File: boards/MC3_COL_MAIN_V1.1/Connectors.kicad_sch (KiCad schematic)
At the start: 11 parts, among them J13 HARNESS_FFC_6P, J3 ENC_leaf1, J4 ENC_leaf2, J5 ENC_leaf3, J6 ENC_leaf4

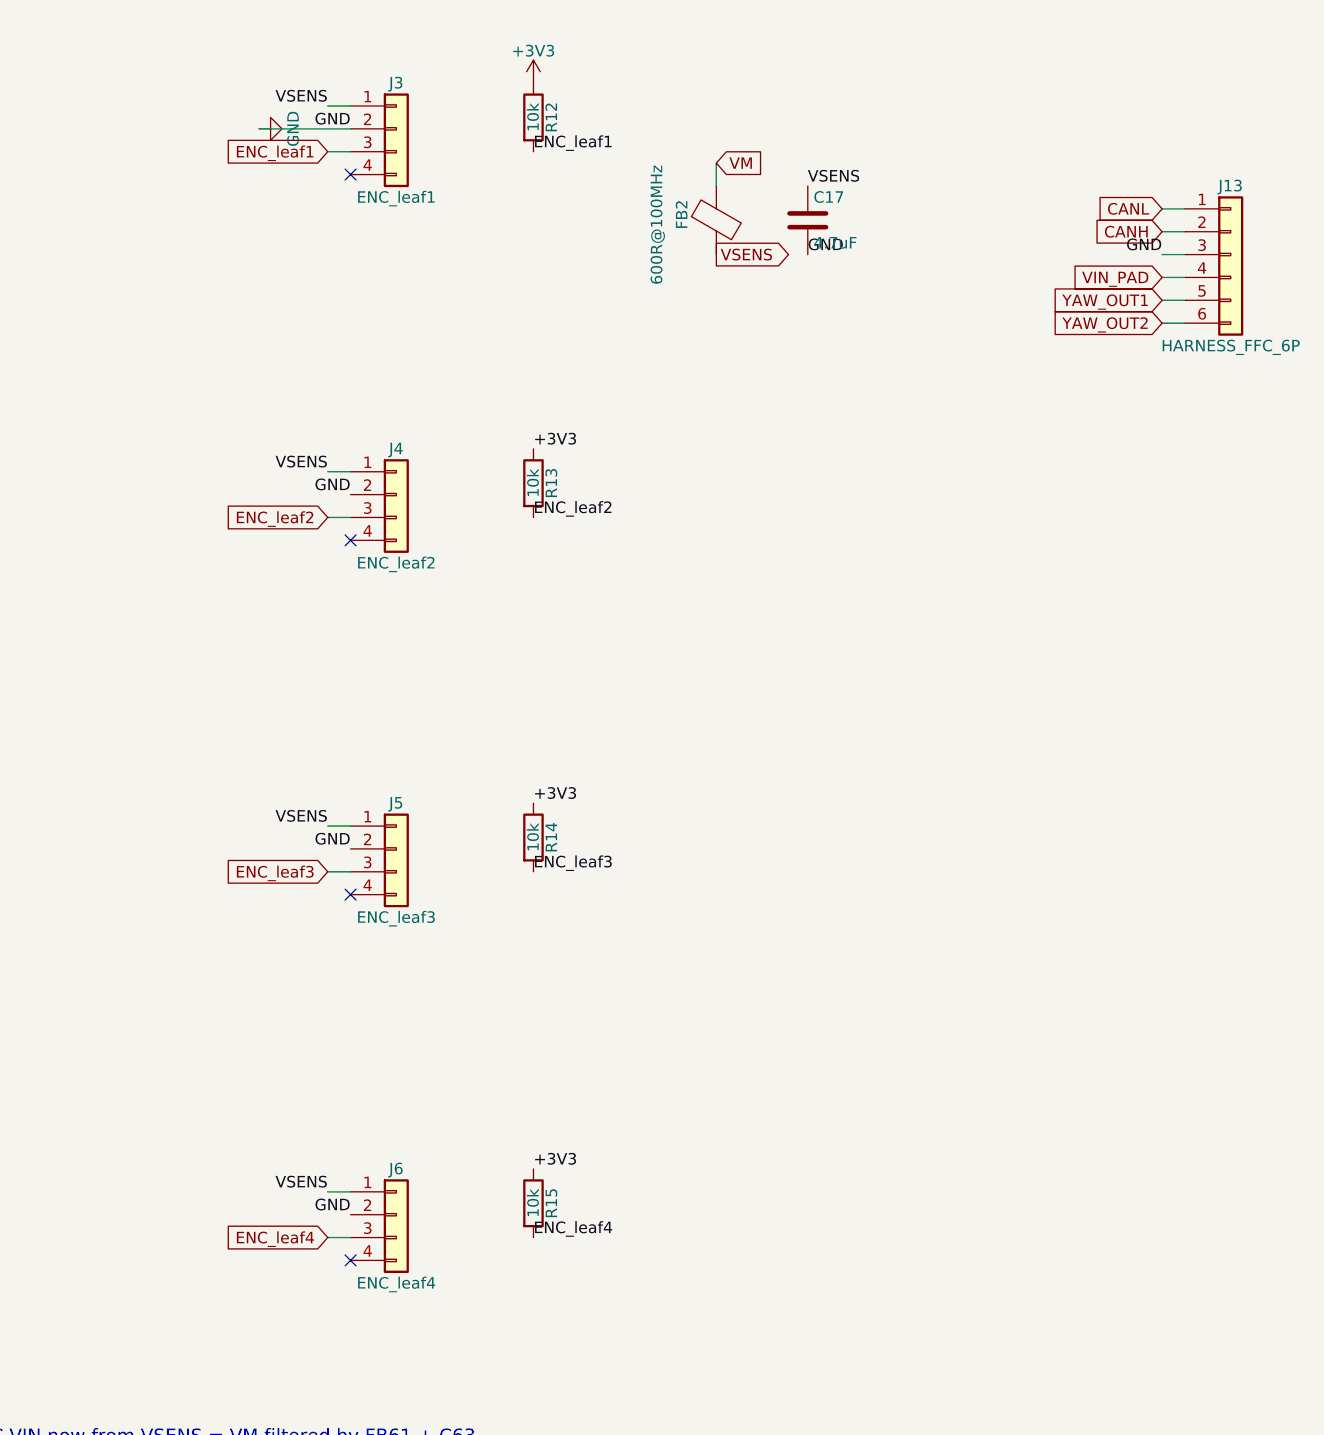
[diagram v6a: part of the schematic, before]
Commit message: V1.1: encoder FFC pin 4 -> RC_OUT_leafN (optical-fallback B channel over the open-drain ripple net); ERC 0 errors
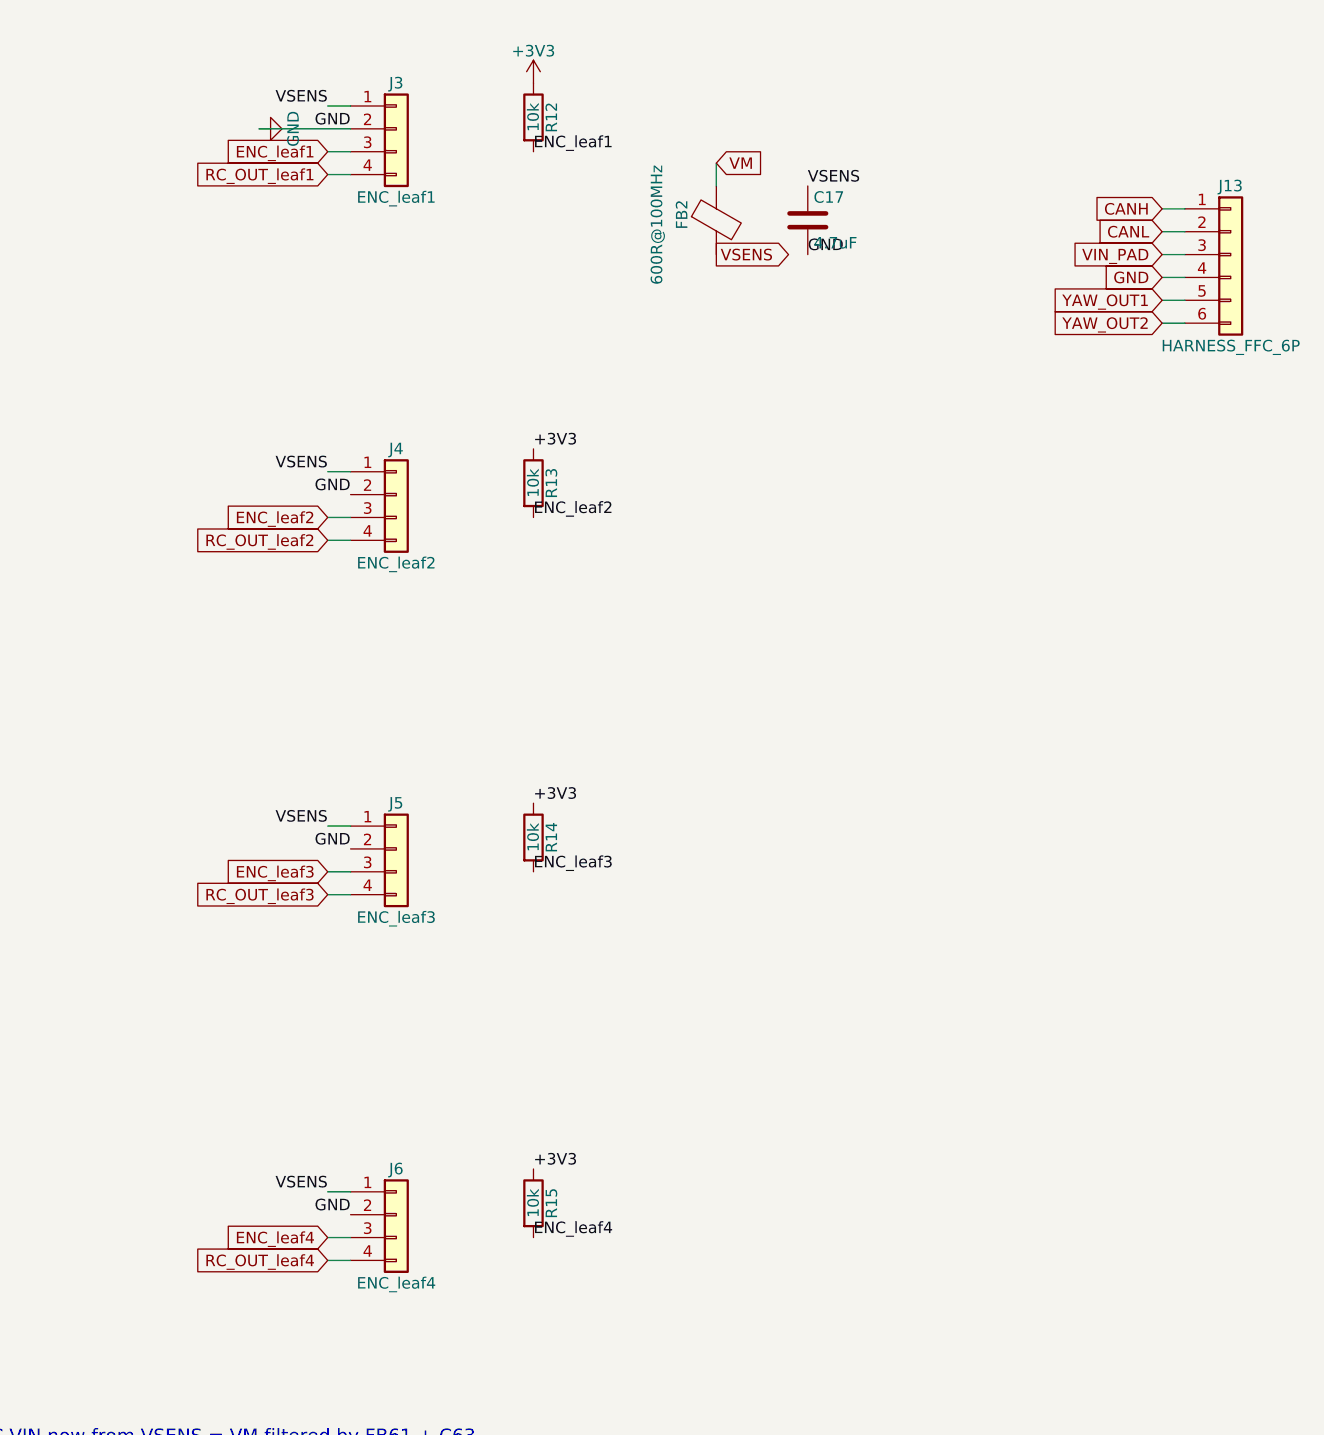
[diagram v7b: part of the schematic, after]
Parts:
- J3: Note Encoder FFC leaf1: 1 VIN(VM) 2 GND 3 SIG 4 spare. Vault: CO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 -> Encoder FFC leaf1. Pin 4 (spare) wired to RC_OUT_leaf1 (202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
- J4: Note Encoder FFC leaf2: 1 VIN(VM) 2 GND 3 SIG 4 spare. Vault: CO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 -> Encoder FFC leaf2. Pin 4 -> RC_OUT_leaf2, dual-mode fallbac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
- J5: Note Encoder FFC leaf3: 1 VIN(VM) 2 GND 3 SIG 4 spare. Vault: CO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 -> Encoder FFC leaf3. Pin 4 -> RC_OUT_leaf3, dual-mode fallbac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
- J6: Note Encoder FFC leaf4: 1 VIN(VM) 2 GND 3 SIG 4 spare. Vault: CO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 -> Encoder FFC leaf4. Pin 4 -> RC_OUT_leaf4, dual-mode fallbac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
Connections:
- net CANH: now also J13.1 (Pin_1); no longer J13.2 (Pin_2)
- net CANL: now also J13.2 (Pin_2); no longer J13.1 (Pin_1)
- net GND: now also J13.4 (Pin_4); no longer J13.3 (Pin_3)
- net VIN_PAD: now also J13.3 (Pin_3); no longer J13.4 (Pin_4)
- net RC_OUT_leaf1: now reaches J3.4 (Pin_4)
- net RC_OUT_leaf4: now reaches J6.4 (Pin_4)
- net RC_OUT_leaf2: now reaches J4.4 (Pin_4)
- net RC_OUT_leaf3: now reaches J5.4 (Pin_4)
- no-connect marks 4 -> 0
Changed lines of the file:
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@@
 	(generator_version "10.0")
 	(paper "A4")
-	(no_connect
-		(at 54.61 134.62)
-	)
-	(no_connect
-		(at 54.61 175.26)
-	)
-	(no_connect
-		(at 54.61 95.25)
-	)
-	(no_connect
-		(at 54.61 54.61)
-	)
 	(wire
 		(pts
@@
 		)
 	)
+	(wire
+		(pts
+			(xy 54.61 54.61)
+			(xy 52.07 54.61)
+		)
+	)
+	(wire
+		(pts
+			(xy 54.61 95.25)
+			(xy 52.07 95.25)
+		)
+	)
+	(wire
+		(pts
+			(xy 54.61 134.62)
+			(xy 52.07 134.62)
+		)
+	)
+	(wire
+		(pts
+			(xy 54.61 175.26)
+			(xy 52.07 175.26)
+		)
+	)
 	(text "Review 2026-08-22: FFC VIN now from VSENS = VM filtered by FB61 + C63."
 		(at 30 195 0)
@@
 			)
 			(justify left bottom)
-		)
-	)
-	(label "GND"
-		(at 144.78 63.5 180)
-		(effects
-			(font
-				(size 1.27 1.27)
-			)
-			(justify right bottom)
 		)
 	)
@@
 		)
 	)
+	(global_label "GND"
+		(shape input)
+		(at 144.78 66.04 180)
+		(effects
+			(font
+				(size 1.27 1.27)
+			)
+			(justify right)
+		)
+		(property "Intersheetrefs" "${INTERSHEET_REFS}"
+			(at 144.78 66.04 0)
+			(hide yes)
+			(show_name no)
+			(do_not_autoplace no)
+			(effects
+				(font
+					(size 1.27 1.27)
+				)
+			)
+		)
+	)
+	(global_label "VIN_PAD"
+		(shape input)
+		(at 144.78 63.5 180)
+		(effects
+			(font
+				(size 1.27 1.27)
+			)
+			(justify right)
+		)
+		(property "Intersheetrefs" "${INTERSHEET_REFS}"
+			(at 144.78 63.5 0)
+			(hide yes)
+			(show_name no)
+			(do_not_autoplace no)
+			(effects
+				(font
+					(size 1.27 1.27)
+				)
+			)
+		)
+	)
+	(global_label "YAW_OUT2"
+		(shape input)
+		(at 144.78 71.12 180)
+		(effects
+			(font
+				(size 1.27 1.27)
+			)
+			(justify right)
+		)
+		(property "Intersheetrefs" "${INTERSHEET_REFS}"
+			(at 144.78 71.12 0)
+			(hide yes)
+			(show_name no)
+			(do_not_autoplace no)
+			(effects
+				(font
+					(size 1.27 1.27)
+				)
+			)
+		)
+	)
 	(global_label "ENC_leaf2"
 		(shape input)
@@
 		)
 	)
+	(global_label "YAW_OUT1"
+		(shape input)
+		(at 144.78 68.58 180)
+		(effects
+			(font
+				(size 1.27 1.27)
+			)
+			(justify right)
+		)
+		(property "Intersheetrefs" "${INTERSHEET_REFS}"
+			(at 144.78 68.58 0)
+			(hide yes)
+			(show_name no)
+			(do_not_autoplace no)
+			(effects
+				(font
+					(size 1.27 1.27)
+				)
+			)
+		)
+	)
 	(global_label "VM"
 		(shape input)
@@
 		)
 	)
+	(global_label "CANL"
+		(shape input)
+		(at 144.78 60.96 180)
+		(effects
+			(font
+				(size 1.27 1.27)
+			)
+			(justify right)
+		)
+		(property "Intersheetrefs" "${INTERSHEET_REFS}"
+			(at 144.78 60.96 0)
+			(hide yes)
+			(show_name no)
+			(do_not_autoplace no)
+			(effects
+				(font
+					(size 1.27 1.27)
+				)
+			)
+		)
+	)
+	(global_label "CANH"
+		(shape input)
+		(at 144.78 58.42 180)
+		(effects
+			(font
+				(size 1.27 1.27)
+			)
+			(justify right)
+		)
+		(property "Intersheetrefs" "${INTERSHEET_REFS}"
+			(at 144.78 58.42 0)
+			(hide yes)
+			(show_name no)
+			(do_not_autoplace no)
+			(effects
+				(font
+					(size 1.27 1.27)
+				)
+			)
+		)
+	)
 	(global_label "ENC_leaf3"
 		(shape input)
@@
 		)
 	)
-	(global_label "CANL"
+	(global_label "RC_OUT_leaf1"
 		(shape input)
-		(at 144.78 58.42 180)
+		(at 52.07 54.61 180)
 		(effects
 			(font
@@
 		)
 	)
-	(global_label "CANH"
+	(global_label "RC_OUT_leaf2"
 		(shape input)
-		(at 144.78 60.96 180)
+		(at 52.07 95.25 180)
 		(effects
 			(font
@@
 		)
 	)
-	(global_label "VIN_PAD"
+	(global_label "RC_OUT_leaf3"
 		(shape input)
-		(at 144.78 66.04 180)
+		(at 52.07 134.62 180)
 		(effects
 			(font
@@
 		)
 	)
-	(global_label "YAW_OUT1"
+	(global_label "RC_OUT_leaf4"
 		(shape input)
-		(at 144.78 68.58 180)
-		(effects
-			(font
-				(size 1.27 1.27)
-			)
-			(justify right)
-		)
-	)
-	(global_label "YAW_OUT2"
-		(shape input)
-		(at 144.78 71.12 180)
+		(at 52.07 175.26 180)
 		(effects
 			(font
@@
 			)
 		)
-		(property "Note" "Encoder FFC leaf1: 1 VIN(VM) 2 GND 3 SIG 4 spare. Vault: COL-COTS-0031, Connectors / Encoder Interface. Right-angle SMD, no solder tabs - the four 0.5mm joints are the only mechanical attachment; footprint mech pads are netless and should be tied to GND"
+		(property "Note" "Encoder FFC leaf1. Pin 4 (spare) wired to RC_OUT_leaf1 (2026-08-27): dual-mode fallback - with the inductive board the pin floats at the far end and the DRV8214 ripple counter owns the net (open-drain); with an AEDR-8300 optical fallback board its B channel drives the net and firmware sets DIS_EC so the DRV releases it. A on pin 3 as before. See Main-Board-01 Encoder Interface s Optical Fallback."
 			(at 59.69 49.53 0)
 			(hide yes)
@@
 			)
 		)
-		(property "Note" "Encoder FFC leaf4: 1 VIN(VM) 2 GND 3 SIG 4 spare. Vault: COL-COTS-0031, Connectors / Encoder Interface"
+		(property "Note" "Encoder FFC leaf4. Pin 4 -> RC_OUT_leaf4, dual-mode fallback - see J3."
 			(at 59.69 170.18 0)
 			(hide yes)
@@
 			)
 		)
-		(property "Note" "Encoder FFC leaf2: 1 VIN(VM) 2 GND 3 SIG 4 spare. Vault: COL-COTS-0031, Connectors / Encoder Interface"
+		(property "Note" "Encoder FFC leaf2. Pin 4 -> RC_OUT_leaf2, dual-mode fallback - see J3."
 			(at 59.69 90.17 0)
 			(hide yes)
@@
 			)
 		)
-		(property "Note" "Encoder FFC leaf3: 1 VIN(VM) 2 GND 3 SIG 4 spare. Vault: COL-COTS-0031, Connectors / Encoder Interface"
+		(property "Note" "Encoder FFC leaf3. Pin 4 -> RC_OUT_leaf3, dual-mode fallback - see J3."
 			(at 59.69 129.54 0)
 			(hide yes)
